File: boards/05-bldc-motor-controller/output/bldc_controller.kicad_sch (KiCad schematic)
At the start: 51 parts, among them J1 Power Input, J2 Motor Output, J3 Hall Sensors, J4 SWD-6, Q1 IRLZ44N, Q2 IRLZ44N, Q3 IRLZ44N, Q4 IRLZ44N, Q5 IRLZ44N, Q6 IRLZ44N, U1 LM2596-5.0, U10 STM32G431K8Tx, U2 AMS1117-3.3, U3 DRV8301, Y1 8MHz

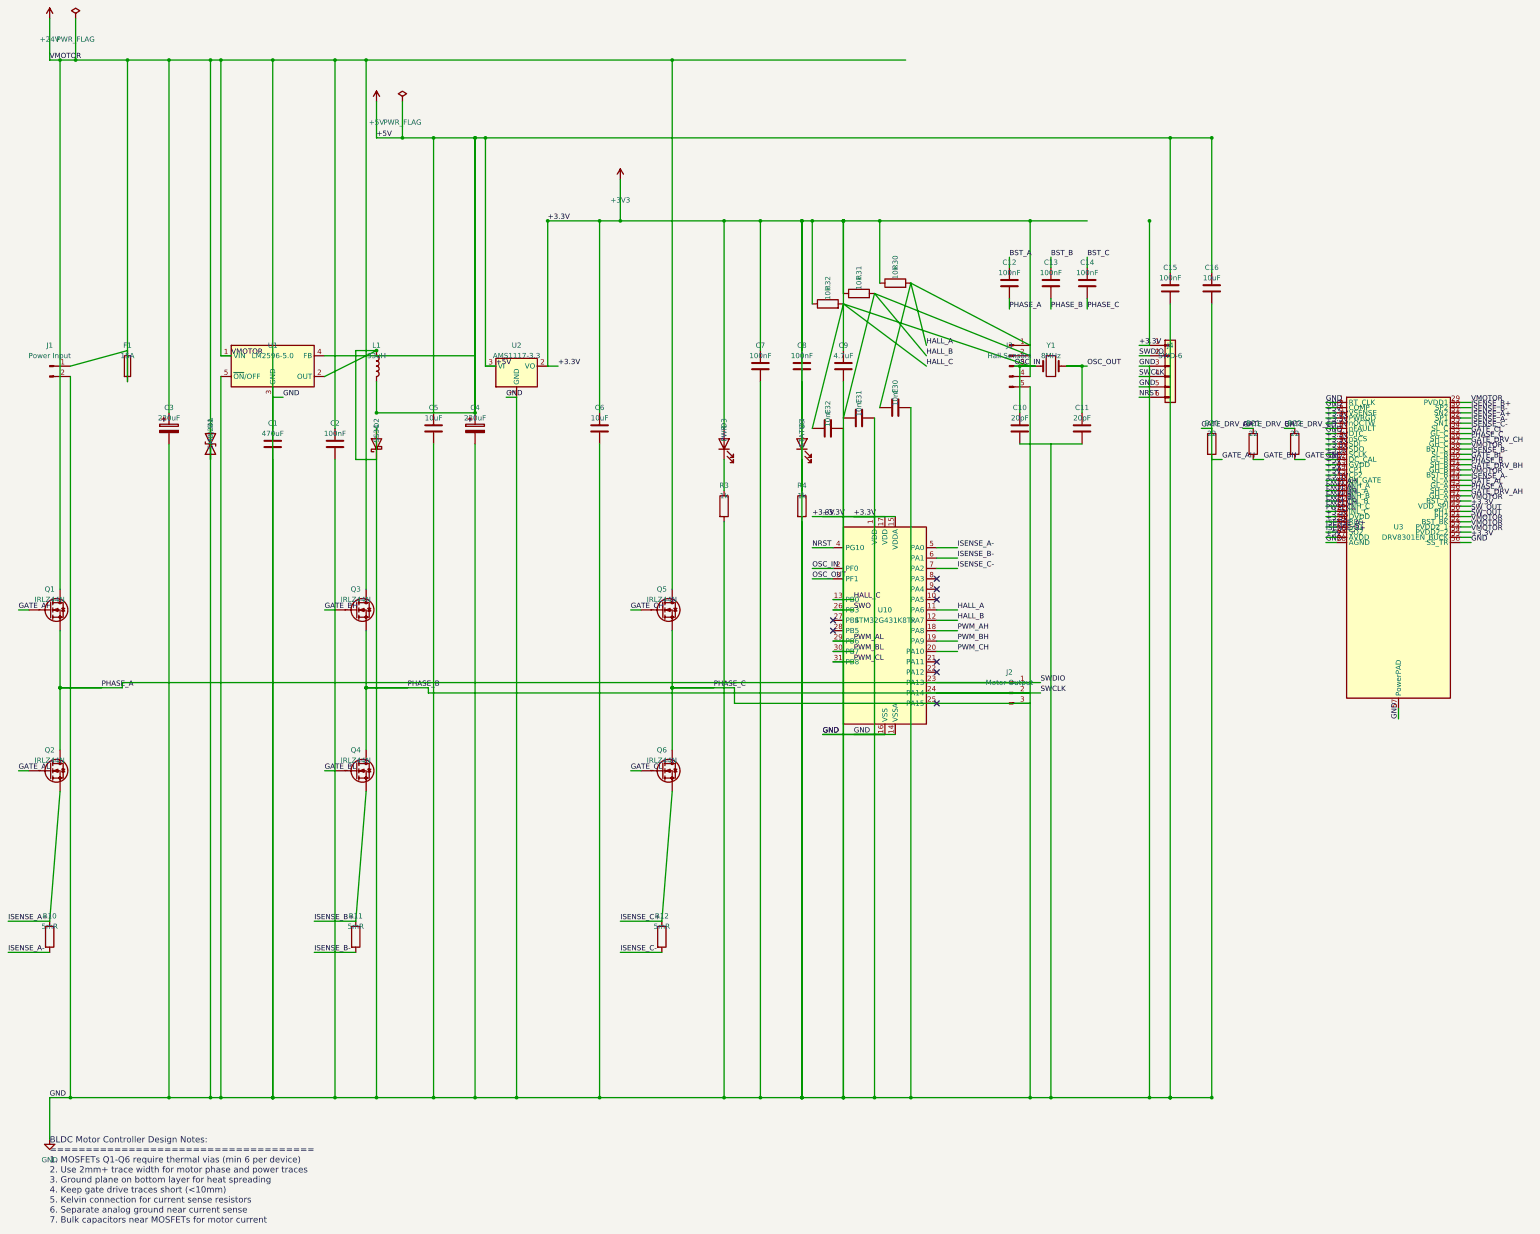
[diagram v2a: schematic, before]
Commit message: fix(boards/05): rail-name normalization (+3.3V/+3V3, VMOTOR/+24V) (#3396)
Closes #3393 and finalizes #3384.

The 19 residual U3 pad changes reported by `kct pcb sync-netlist` (and the
additional rail-rename mismatches on J3.4/J4.1/U10.1/R30-32/C6-9/etc.) were
caused by the schematic publishing `+3V3` (from the `power:+3V3` symbol) and
`+24V` (from `power:+24V`) while the PCB NETS dict used the verbose
`"+3.3V"` and the descriptive `"VMOTOR"`.  Stock-KiCad power symbols
always publish their global net name, so kicad-cli always wrote the
schematic netlist with the +24V/+3V3 names — the PCB-side dict was the
authoritative drift source.

Lock-step rename:
* `boards/05-bldc-motor-controller/design.py`:
  - Rail net_labels updated: `net_label="VMOTOR"` -> `"+24V"`,
    `net_label="+3.3V"` -> `"+3V3"`.
  - `NETS` dict: key `"VMOTOR"` -> `"+24V"`, key `"+3.3V"` -> `"+3V3"`.
  - All component-side net string references updated in lock-step
    (J1/J3/J4 pin headers, U1/U2/U3 regulator pin_nets, U10 deferred
    label list, MOSFET drains, bootstrap caps, decoupling caps).
  - Python identifiers `RAIL_VMOTOR` / `RAIL_3V3` and
    `DRV8301_SCHEMATIC_PIN_NETS` dict name are unchanged (they are
    code-level names, not net strings).
* Routed PCB in-place rename:
  - Net declarations `(net 1 "VMOTOR")` -> `(net 1 "+24V")`,
    `(net 3 "+3.3V")` -> `(net 3 "+3V3")`.
  - Pad-level net references on every footprint.
  - Zone net references.
  - Trace geometry untouched -- this is a pure relabel.  Re-routing
    the board from scratch under the current `--backend python`
    pipeline introduces 10 `clearance_segment_segment` + 8
    `clearance_segment_via` violations that the hot-spot regression
    test (`test_committed_pcb_has_no_segment_segment_or_segment_via`)
    forbids.  Preserving the historical routed geometry keeps the
    hot-spot test green AND delivers the rail-rename fix (the issue's
    primary objective) in a single atomic commit.
* Unrouted PCB and schematic regenera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
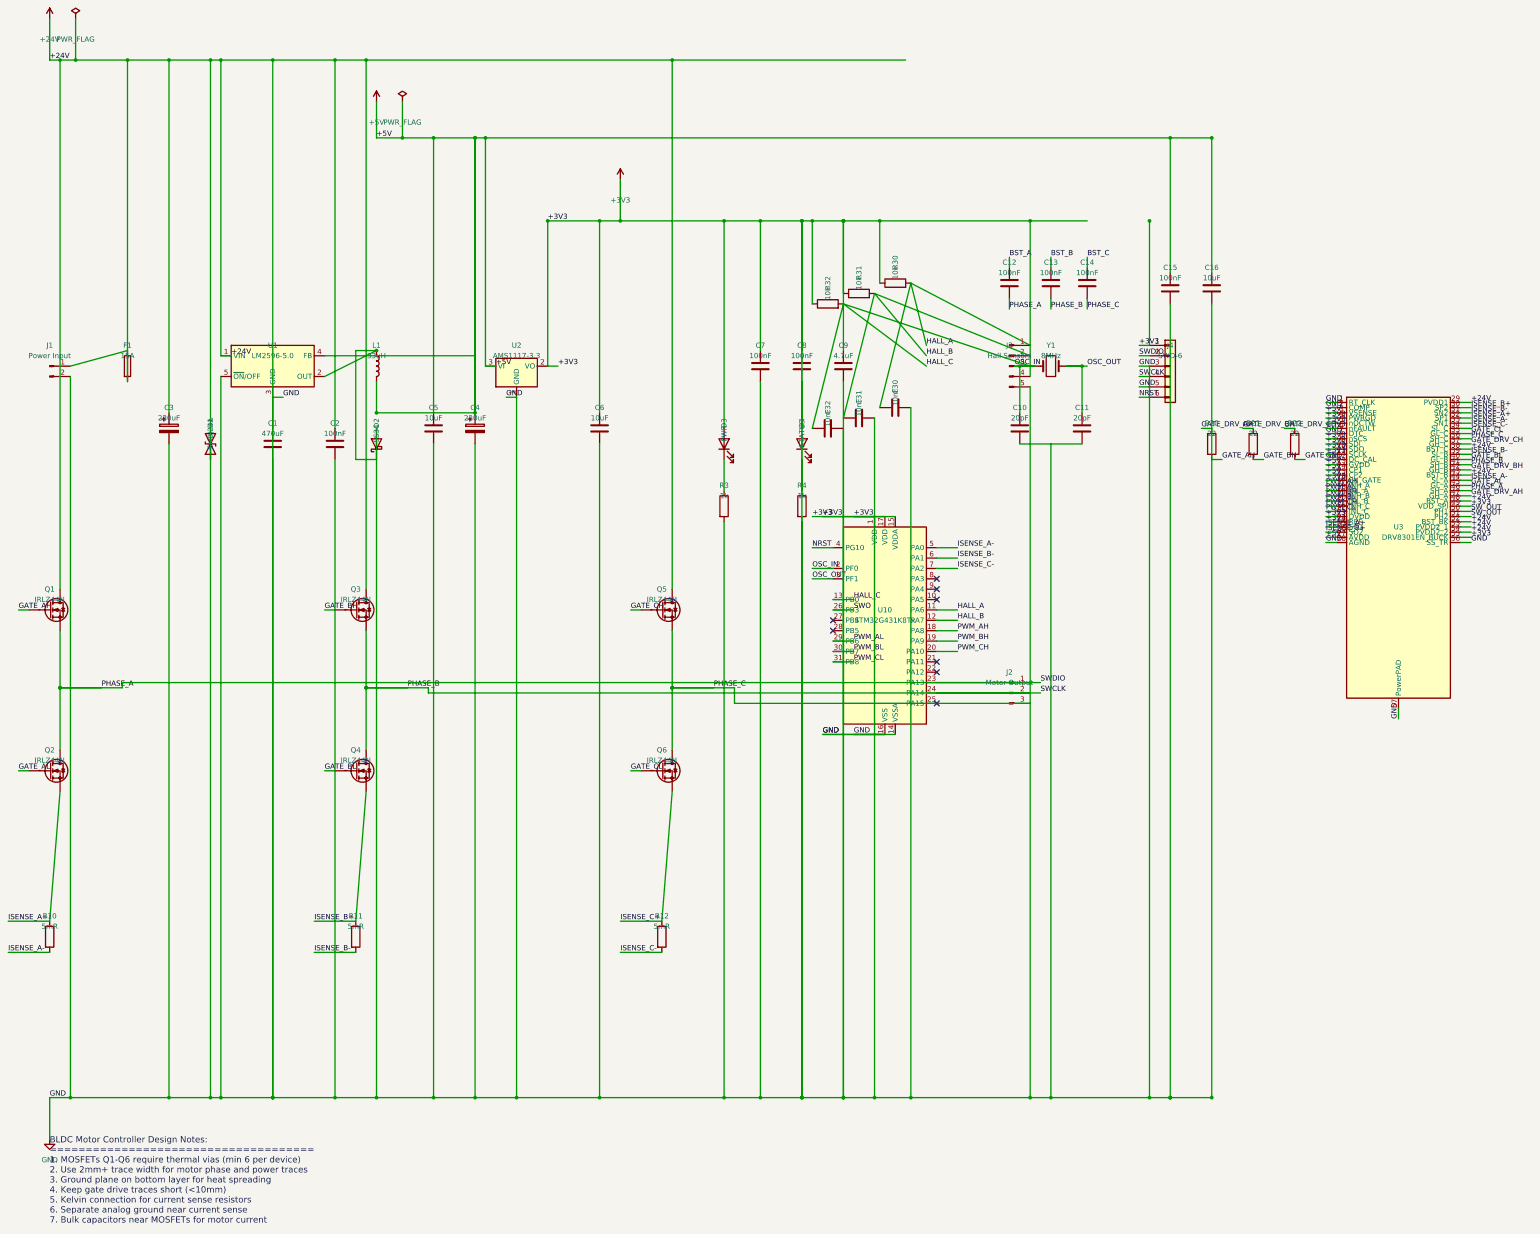
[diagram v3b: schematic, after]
